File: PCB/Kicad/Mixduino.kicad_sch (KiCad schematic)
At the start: 4 parts

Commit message: routing
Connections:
- net SIG_PAD_LED_R is gone; now on net SWPAD-L4: XA1.D46
- net SWPAD-L4: no longer XA1.D23
- net NP_SIG_LEFT: now reaches XA1.D2 (D2_INT0)
- net SWSEL-L1 renamed SW-DECK-SEL
- new net NP_SIG_RIGTH: XA1.D23
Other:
- sheet PadLedsSheet renamed NeoPixelsSheet
- sheet NeoPixelsSheet: file pad-leds.kicad_sch -> neopixels.kicad_sch

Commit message: more routing
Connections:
- net SIG_PAD_LED_L is gone; now on net SWPAD-L5: XA1.D0 (D0_RX0)
- net SWCUE-L: now also XA1.D22; no longer XA1.D1 (D1_TX0)
- net SWPAD-L2: now also XA1.D19 (D19_RX1); no longer XA1.D22
- net SWPAD-L5: no longer XA1.D14 (D14_TX3)
- net SWPAD-L8: now also XA1.D1 (D1_TX0); no longer XA1.D19 (D19_RX1)

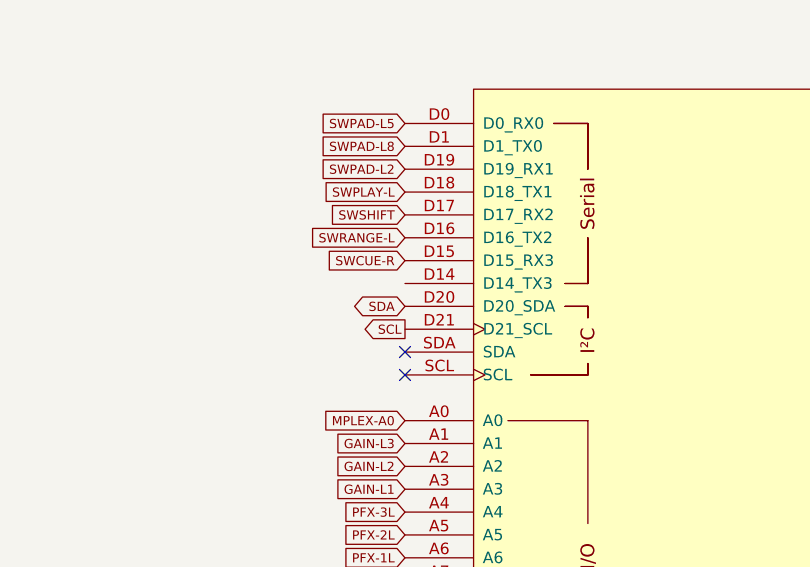
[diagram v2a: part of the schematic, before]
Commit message: removed neopixel capacitors
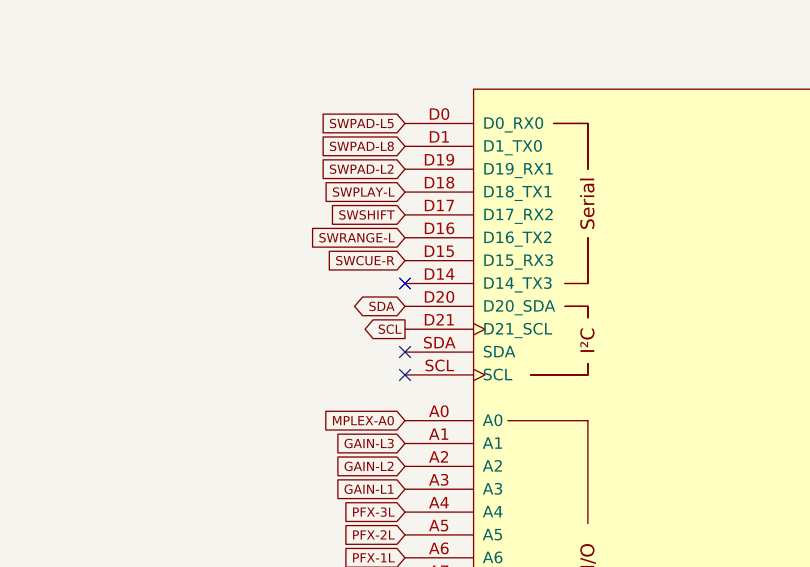
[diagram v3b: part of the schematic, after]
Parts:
- IC-POTS-1: symbol SamacSys_Parts:74HC4067D,653 -> mixduino-mk2:74HC4067D,653
- XA1: symbol arduino:Arduino_Mega2560_Shield -> mixduino-mk2:Arduino_Mega2560_Shield
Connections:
- no-connect marks 9 -> 10
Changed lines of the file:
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@@
 (kicad_sch (version 20210406) (generator eeschema)
   (paper "A4")
+  (no_connect (at 127.635 57.15))
   (no_connect (at 127.635 64.77))
   (no_connect (at 127.635 67.31))
@@
     (pin "1")
   )
-  (symbol (lib_id "mixduino-mk2:trillbar") (at 102.87 180.975 0) (mirror y) (unit 1)
+  (symbol (lib_name "mixduino-mk2:trillbar_1") (lib_id "mixduino-mk2:trillbar") (at 102.87 180.975 0) (mirror y) (unit 1)
     (in_bom yes) (on_board yes)
     (property "Reference" "TB1" (id 0) (at 100.965 166.3699 0)
@@
     (pin "4")
   )
-  (symbol (lib_id "SamacSys_Parts:74HC4067D,653") (at 236.855 121.92 0) (unit 1)
+  (symbol (lib_id "mixduino-mk2:74HC4067D,653") (at 236.855 121.92 0) (unit 1)
     (in_bom yes) (on_board yes)
     (property "Reference" "IC-POTS-1" (id 0) (at 249.555 115.57 0))
@@
     (pin "9")
   )
-  (symbol (lib_id "arduino:Arduino_Mega2560_Shield") (at 160.655 93.98 0) (unit 1)
+  (symbol (lib_id "mixduino-mk2:Arduino_Mega2560_Shield") (at 160.655 93.98 0) (unit 1)
     (in_bom yes) (on_board yes)
     (property "Reference" "XA1" (id 0) (at 160.655 154.94 0)
@@
       (reference "UVU-MASTER-R1") (unit 1) (value "74HC595") (footprint "Library:SO-16_3.9x9.9mm_P1.27mm")
     )
-    (path "/27ec6e33-6a27-4865-8f8e-aab38be2398e/beadbaa6-fcf7-4c3f-81c0-a74b13dde53a"
-      (reference "C1") (unit 1) (value "100nF") (footprint "Library:C_1206_3216Metric_Pad1.33x1.80mm_HandSolder")
-    )
-    (path "/27ec6e33-6a27-4865-8f8e-aab38be2398e/f7af72b4-7423-4bf3-8c0a-b10a734d692a"
-      (reference "C2") (unit 1) (value "100nF") (footprint "Library:C_1206_3216Metric_Pad1.33x1.80mm_HandSolder")
-    )
-    (path "/27ec6e33-6a27-4865-8f8e-aab38be2398e/82fc8588-4785-4200-bb02-8896037f53f6"
-      (reference "C3") (unit 1) (value "100nF") (footprint "Library:C_1206_3216Metric_Pad1.33x1.80mm_HandSolder")
-    )
-    (path "/27ec6e33-6a27-4865-8f8e-aab38be2398e/bfdd7e18-30e1-44ba-83d8-f528e8d9ba6c"
-      (reference "C4") (unit 1) (value "100nF") (footprint "Library:C_1206_3216Metric_Pad1.33x1.80mm_HandSolder")
-    )
-    (path "/27ec6e33-6a27-4865-8f8e-aab38be2398e/1987203e-8e13-40ac-9d11-2f95e6f9d5d4"
-      (reference "C5") (unit 1) (value "100nF") (footprint "Library:C_1206_3216Metric_Pad1.33x1.80mm_HandSolder")
-    )
-    (path "/27ec6e33-6a27-4865-8f8e-aab38be2398e/68b1d9eb-a14b-4b7c-80fc-5da6be6089b5"
-      (reference "C6") (unit 1) (value "100nF") (footprint "Library:C_1206_3216Metric_Pad1.33x1.80mm_HandSolder")
-    )
-    (path "/27ec6e33-6a27-4865-8f8e-aab38be2398e/9e58909a-51f6-4a54-b1ec-5609ac5bcfab"
-      (reference "C7") (unit 1) (value "100nF") (footprint "Library:C_1206_3216Metric_Pad1.33x1.80mm_HandSolder")
-    )
-    (path "/27ec6e33-6a27-4865-8f8e-aab38be2398e/90ca56f2-69c7-47bb-99f2-3236a45bab1d"
-      (reference "C8") (unit 1) (value "100nF") (footprint "Library:C_1206_3216Metric_Pad1.33x1.80mm_HandSolder")
-    )
-    (path "/27ec6e33-6a27-4865-8f8e-aab38be2398e/08e6382b-ae15-4e7c-98e7-34680eac45f0"
-      (reference "C9") (unit 1) (value "100nF") (footprint "Library:C_1206_3216Metric_Pad1.33x1.80mm_HandSolder")
-    )
-    (path "/27ec6e33-6a27-4865-8f8e-aab38be2398e/933308c1-72b0-4bdc-ba47-e4dda7ad16ea"
-      (reference "C10") (unit 1) (value "100nF") (footprint "Library:C_1206_3216Metric_Pad1.33x1.80mm_HandSolder")
-    )
-    (path "/27ec6e33-6a27-4865-8f8e-aab38be2398e/b383111b-b145-4f6f-8d5c-dfe94062ce09"
-      (reference "C11") (unit 1) (value "100nF") (footprint "Library:C_1206_3216Metric_Pad1.33x1.80mm_HandSolder")
-    )
-    (path "/27ec6e33-6a27-4865-8f8e-aab38be2398e/b80e4604-0f34-4a2c-ada8-f246527215e2"
-      (reference "C12") (unit 1) (value "100nF") (footprint "Library:C_1206_3216Metric_Pad1.33x1.80mm_HandSolder")
-    )
-    (path "/27ec6e33-6a27-4865-8f8e-aab38be2398e/b7864320-d3e4-4df5-b673-3366141f9299"
-      (reference "C13") (unit 1) (value "100nF") (footprint "Library:C_1206_3216Metric_Pad1.33x1.80mm_HandSolder")
-    )
-    (path "/27ec6e33-6a27-4865-8f8e-aab38be2398e/d916989c-d7c8-4376-a8f8-20874c66e37e"
-      (reference "C14") (unit 1) (value "100nF") (footprint "Library:C_1206_3216Metric_Pad1.33x1.80mm_HandSolder")
-    )
-    (path "/27ec6e33-6a27-4865-8f8e-aab38be2398e/c3464658-7739-4302-9d41-54ee61cd0504"
-      (reference "C15") (unit 1) (value "100nF") (footprint "Library:C_1206_3216Metric_Pad1.33x1.80mm_HandSolder")
-    )
-    (path "/27ec6e33-6a27-4865-8f8e-aab38be2398e/73e95c03-44ce-45eb-9038-d59afccad52d"
-      (reference "C16") (unit 1) (value "100nF") (footprint "Library:C_1206_3216Metric_Pad1.33x1.80mm_HandSolder")
-    )
-    (path "/27ec6e33-6a27-4865-8f8e-aab38be2398e/b2905d81-053d-4b55-9c94-1ca48ddb8c3f"
-      (reference "C17") (unit 1) (value "100nF") (footprint "Library:C_1206_3216Metric_Pad1.33x1.80mm_HandSolder")
-    )
-    (path "/27ec6e33-6a27-4865-8f8e-aab38be2398e/8a8718ca-1aad-4e99-96f7-bc0f2aa37fd4"
-      (reference "C18") (unit 1) (value "100nF") (footprint "Library:C_1206_3216Metric_Pad1.33x1.80mm_HandSolder")
-    )
-    (path "/27ec6e33-6a27-4865-8f8e-aab38be2398e/50bca312-9f3e-46ad-8e33-8efc305e5cb9"
-      (reference "C19") (unit 1) (value "100nF") (footprint "Library:C_1206_3216Metric_Pad1.33x1.80mm_HandSolder")
-    )
-    (path "/27ec6e33-6a27-4865-8f8e-aab38be2398e/fe5e5206-6a4d-4884-bd30-a819cc90269f"
-      (reference "C20") (unit 1) (value "100nF") (footprint "Library:C_1206_3216Metric_Pad1.33x1.80mm_HandSolder")
-    )
-    (path "/27ec6e33-6a27-4865-8f8e-aab38be2398e/ccf6e1ed-7848-4d1b-87f8-537ea377ff57"
-      (reference "C21") (unit 1) (value "100nF") (footprint "Library:C_1206_3216Metric_Pad1.33x1.80mm_HandSolder")
-    )
     (path "/27ec6e33-6a27-4865-8f8e-aab38be2398e/df118aaf-5864-4327-8260-83fd890ea0c8"
